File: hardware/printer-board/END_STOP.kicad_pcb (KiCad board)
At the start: 2 copper layers, 18 parts, among them J26 X_MIN, J27 X_MAX, J28 Y_MIN, J29 Y_MAX, J30 Z_MIN, J31 Z_MAX

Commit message: update,
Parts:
- J26, J27, J28, J29, J30, J31: footprint footprint-lib:s3b-ph-kl,end_stop -> footprint-lib:b3b-ph-kl,end_stop
- moved J29 22.7 mm to (27.8, 50.2), turned to 180 degrees
- moved J31 22.1 mm to (38.0, 50.2), turned to 180 degrees
- moved D20 17.5 mm to (43.0, 49.7)
- moved R64 17.5 mm to (43.0, 49.7)
- moved D18 14.0 mm to (33.0, 49.6)
- moved R62 14.0 mm to (33.0, 49.6)
- moved J30 12.7 mm to (38.1, 43.6), turned to 180 degrees
- moved J28 12.3 mm to (27.9, 43.8), turned to 180 degrees
- moved J27 11.7 mm to (27.9, 37.0), turned to 180 degrees
- moved D17 11.5 mm to (33.0, 43.4)
- moved R61 11.5 mm to (33.0, 43.4)
- moved J26 11.0 mm to (28.1, 31.5), turned to 180 degrees
- moved R59 9.83 mm to (33.2, 31.2)
- moved D16 9.66 mm to (33.2, 36.9)
- moved R60 9.66 mm to (33.2, 36.9)
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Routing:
- net +5V: track 51.7 -> 0.00 mm
- net GND: track 51.0 -> 0.00 mm
- net /Y_MIN: track 4.47 -> 0.00 mm
- net /Z_MAX: track 4.26 -> 0.00 mm
- net /Y_MAX: track 4.17 -> 0.00 mm
- net /X_MIN: track 4.16 -> 0.00 mm
- net /Z_MIN: track 3.97 -> 0.00 mm
- net /X_MAX: track 3.55 -> 0.00 mm
- net Net-(D15-Pad2): track 2.98 -> 0.00 mm, vias 1 -> 0
- net Net-(D16-Pad2): track 2.90 -> 0.00 mm, vias 1 -> 0
- net Net-(D18-Pad2): track 2.47 -> 0.00 mm, vias 1 -> 0
- net Net-(D20-Pad2): track 2.27 -> 0.00 mm, vias 1 -> 0
- net Net-(D19-Pad2): track 2.24 -> 0.00 mm, vias 1 -> 0
- net Net-(D17-Pad2): track 2.22 -> 0.00 mm, vias 1 -> 0

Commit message: update for stepper Z,
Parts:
- added C1: CP100uf,35V, Capacitor_SMD:C_0603_1608Metric_Pad1.05x0.95mm_HandSolder, F.Cu at (190.6, 45.3)
- added C10: CP100uf,25V, Capacitor_SMD:CP_Elec_6.3x7.7, F.Cu at (297.3, 53.2)
- added C11: C104,0603, Capacitor_SMD:C_0603_1608Metric_Pad1.05x0.95mm_HandSolder, F.Cu at (297.6, 59.1)
- added C12: CP100uf,25V, Capacitor_SMD:CP_Elec_6.3x7.7, F.Cu at (240.3, 109.1)
- added C13: C104,0603, Capacitor_SMD:C_0603_1608Metric_Pad1.05x0.95mm_HandSolder, F.Cu at (237.3, 115.0)
- added C14: C106,0603, Capacitor_SMD:C_0603_1608Metric_Pad1.05x0.95mm_HandSolder, F.Cu at (295.6, 127.7)
- added C15: C106,0603, Capacitor_SMD:C_0603_1608Metric_Pad1.05x0.95mm_HandSolder, F.Cu at (292.3, 136.8)
- added C16: C106,0603, Capacitor_SMD:C_0603_1608Metric_Pad1.05x0.95mm_HandSolder, F.Cu at (292.3, 127.7)
- added C17: C106,0603, Capacitor_SMD:C_0603_1608Metric_Pad1.05x0.95mm_HandSolder, F.Cu at (295.6, 129.2)
- added C18: C106,0603, Capacitor_SMD:C_0603_1608Metric_Pad1.05x0.95mm_HandSolder, F.Cu at (292.3, 132.3)
- added C19: C104,0603, Capacitor_SMD:C_0603_1608Metric_Pad1.05x0.95mm_HandSolder, F.Cu at (221.4, 140.3)
- added C2: CP100uf,25V, Capacitor_SMD:CP_Elec_6.3x7.7, F.Cu at (160.0, 109.1)
- added C20: CP100uf,35V, Capacitor_SMD:CP_Elec_6.3x7.7, F.Cu at (235.1, 137.6)
- added C21: C104,0603, Capacitor_SMD:C_0603_1608Metric_Pad1.05x0.95mm_HandSolder, F.Cu at (295.3, 86.0)
- added C22: C10pf,0603, Capacitor_SMD:C_0603_1608Metric_Pad1.05x0.95mm_HandSolder, F.Cu at (281.9, 85.8)
- added C23: C104,0603, Capacitor_SMD:C_0603_1608Metric_Pad1.05x0.95mm_HandSolder, F.Cu at (308.3, 76.8)
- added C24: C10pf,0603, Capacitor_SMD:C_0603_1608Metric_Pad1.05x0.95mm_HandSolder, F.Cu at (285.2, 85.8)
- added C25: C104,0603, Capacitor_SMD:C_0603_1608Metric_Pad1.05x0.95mm_HandSolder, F.Cu at (295.1, 82.0)
- added C26: C104,0603, Capacitor_SMD:C_0603_1608Metric_Pad1.05x0.95mm_HandSolder, F.Cu at (295.1, 80.4)
- added C27: C104,0603, Capacitor_SMD:C_0603_1608Metric_Pad1.05x0.95mm_HandSolder, F.Cu at (298.5, 80.4)
- added C28: C104,0603, Capacitor_SMD:C_0603_1608Metric_Pad1.05x0.95mm_HandSolder, F.Cu at (295.1, 83.5)
- added C29: C105,0603, Capacitor_SMD:C_0603_1608Metric_Pad1.05x0.95mm_HandSolder, F.Cu at (305.0, 75.3)
- added C3: C104,0603, Capacitor_SMD:C_0603_1608Metric_Pad1.05x0.95mm_HandSolder, F.Cu at (166.4, 109.9)
- added C30: C104,0603, Capacitor_SMD:C_0603_1608Metric_Pad1.05x0.95mm_HandSolder, F.Cu at (298.5, 78.9)
- added C31: C104,0603, Capacitor_SMD:C_0603_1608Metric_Pad1.05x0.95mm_HandSolder, F.Cu at (291.9, 85.8)
- added C32: C104,0603, Capacitor_SMD:C_0603_1608Metric_Pad1.05x0.95mm_HandSolder, F.Cu at (288.6, 85.8)
- added C33: CP220uf,16V, Capacitor_SMD:C_0603_1608Metric_Pad1.05x0.95mm_HandSolder, F.Cu at (147.7, 149.0)
- added C34: CP220uf,16V, Capacitor_SMD:C_0603_1608Metric_Pad1.05x0.95mm_HandSolder, F.Cu at (144.3, 149.0)
- added C35: CP220uf,25V, Capacitor_SMD:C_0603_1608Metric_Pad1.05x0.95mm_HandSolder, F.Cu at (144.3, 150.5)
- added C36: CP100uf,16V, Capacitor_SMD:CP_Elec_6.3x5.3, F.Cu at (259.2, 130.5)
- added C37: CP100uf,16V, Capacitor_SMD:CP_Elec_6.3x5.3, F.Cu at (321.8, 48.1)
- added C38: CP100uf,16V, Capacitor_SMD:CP_Elec_6.3x5.3, F.Cu at (259.2, 145.1)
- added C39: CP100uf,25V, Capacitor_SMD:CP_Elec_6.3x7.7, F.Cu at (257.2, 77.0)
- added C4: CP100uf,25V, Capacitor_SMD:CP_Elec_6.3x7.7, F.Cu at (200.2, 109.1)
- added C40: C104,0603, Capacitor_SMD:C_0603_1608Metric_Pad1.05x0.95mm_HandSolder, F.Cu at (254.2, 84.5)
- added C41: CP100uf,25V, Capacitor_SMD:CP_Elec_6.3x7.7, F.Cu at (257.2, 53.2)
- added C42: C104,0603, Capacitor_SMD:C_0603_1608Metric_Pad1.05x0.95mm_HandSolder, F.Cu at (263.6, 54.0)
- added C43: C104,0603, Capacitor_SMD:C_0603_1608Metric_Pad1.05x0.95mm_HandSolder, F.Cu at (274.0, 103.0)
- added C44: CP100uf,16V, Capacitor_SMD:CP_Elec_6.3x5.3, F.Cu at (280.3, 95.8)
- added C45: C106,0603, Capacitor_SMD:C_0603_1608Metric_Pad1.05x0.95mm_HandSolder, F.Cu at (318.6, 92.3)
- added C46: C104,0603, Capacitor_SMD:C_0603_1608Metric_Pad1.05x0.95mm_HandSolder, F.Cu at (325.3, 92.3)
- added C47: C332,0603, Capacitor_SMD:C_0603_1608Metric_Pad1.05x0.95mm_HandSolder, F.Cu at (322.0, 92.3)
- added C48: C103,0603, Capacitor_SMD:C_0603_1608Metric_Pad1.05x0.95mm_HandSolder, F.Cu at (318.6, 93.8)
- added C49: C226,6.3v,0603, Capacitor_SMD:C_0603_1608Metric_Pad1.05x0.95mm_HandSolder, F.Cu at (328.7, 93.8)
- added C5: C104,0603, Capacitor_SMD:C_0603_1608Metric_Pad1.05x0.95mm_HandSolder, F.Cu at (197.2, 116.6)
- added C50: C106,0603, Capacitor_SMD:C_0603_1608Metric_Pad1.05x0.95mm_HandSolder, F.Cu at (224.8, 152.9)
- added C51: C104,0603, Capacitor_SMD:C_0603_1608Metric_Pad1.05x0.95mm_HandSolder, F.Cu at (228.1, 151.4)
- added C52: C332,0603, Capacitor_SMD:C_0603_1608Metric_Pad1.05x0.95mm_HandSolder, F.Cu at (221.4, 152.9)
- added C53: C103,0603, Capacitor_SMD:C_0603_1608Metric_Pad1.05x0.95mm_HandSolder, F.Cu at (224.8, 151.4)
- added C54: C226,6.3v,0603, Capacitor_SMD:C_0603_1608Metric_Pad1.05x0.95mm_HandSolder, F.Cu at (221.4, 151.4)
- added C6: CP100uf,25V, Capacitor_SMD:CP_Elec_6.3x7.7, F.Cu at (160.0, 133.1)
- added C7: C104,0603, Capacitor_SMD:C_0603_1608Metric_Pad1.05x0.95mm_HandSolder, F.Cu at (160.3, 139.0)
- added C8: CP100uf,25V, Capacitor_SMD:CP_Elec_6.3x7.7, F.Cu at (200.1, 133.1)
- added C9: C104,0603, Capacitor_SMD:C_0603_1608Metric_Pad1.05x0.95mm_HandSolder, F.Cu at (197.1, 140.5)
- added D1: 5V HEALTHY, LED_SMD:LED_0603_1608Metric_Pad1.05x0.95mm_HandSolder, F.Cu at (141.2, 93.6)
- added D10: LED_BLUE,0603, LED_SMD:LED_0603_1608Metric_Pad1.05x0.95mm_HandSolder, F.Cu at (315.2, 79.3)
- added D11: LED_BLUE,0603, LED_SMD:LED_0603_1608Metric_Pad1.05x0.95mm_HandSolder, F.Cu at (318.6, 79.3)
- added D12: LED_BLUE,0603, LED_SMD:LED_0603_1608Metric_Pad1.05x0.95mm_HandSolder, F.Cu at (318.6, 80.9)
- added D13: LED_BLUE,0603, LED_SMD:LED_0603_1608Metric_Pad1.05x0.95mm_HandSolder, F.Cu at (325.4, 79.3)
- added D14: LED_BLUE,0603, LED_SMD:LED_0603_1608Metric_Pad1.05x0.95mm_HandSolder, F.Cu at (322.0, 79.3)
- added D2: LED_BLUE,0603, LED_SMD:LED_0603_1608Metric_Pad1.05x0.95mm_HandSolder, F.Cu at (157.0, 115.4)
- added D21: LED_BLUE,0603, LED_SMD:LED_0603_1608Metric_Pad1.05x0.95mm_HandSolder, F.Cu at (322.4, 52.4)
- added D22: LED_BLUE,0603, LED_SMD:LED_0603_1608Metric_Pad1.05x0.95mm_HandSolder, F.Cu at (272.1, 142.3)
- added D23: LED_BLUE,0603, LED_SMD:LED_0603_1608Metric_Pad1.05x0.95mm_HandSolder, F.Cu at (254.2, 81.4)
- added D24: LED_BLUE,0603, LED_SMD:LED_0603_1608Metric_Pad1.05x0.95mm_HandSolder, F.Cu at (254.2, 57.5)
- added D3: LED_BLUE,0603, LED_SMD:LED_0603_1608Metric_Pad1.05x0.95mm_HandSolder, F.Cu at (197.2, 113.5)
- added D4: LED_BLUE,0603, LED_SMD:LED_0603_1608Metric_Pad1.05x0.95mm_HandSolder, F.Cu at (157.0, 137.4)
- added D5: LED_BLUE,0603, LED_SMD:LED_0603_1608Metric_Pad1.05x0.95mm_HandSolder, F.Cu at (197.1, 137.4)
- added D6: LED_BLUE,0603, LED_SMD:LED_0603_1608Metric_Pad1.05x0.95mm_HandSolder, F.Cu at (294.3, 57.5)
- added D7: LED_BLUE,0603, LED_SMD:LED_0603_1608Metric_Pad1.05x0.95mm_HandSolder, F.Cu at (237.3, 113.5)
- added D8: LED_RED,0603, LED_SMD:LED_0603_1608Metric_Pad1.05x0.95mm_HandSolder, F.Cu at (295.3, 119.1)
- added D9: LED_BLUE,0603, LED_SMD:LED_0603_1608Metric_Pad1.05x0.95mm_HandSolder, F.Cu at (315.2, 80.9)
- added F1: 16V/30A, w_misc_comp:fuse_smf, F.Cu at (225.0, 127.0)
- added F2: 30V/5A, w_misc_comp:fuse_smf, F.Cu at (225.0, 132.4)
- added H1: MOUNT_M3, MountingHole:MountingHole_2.7mm_M2.5, F.Cu at (3.00, 3.00)
- added H2: MOUNT_M3, MountingHole:MountingHole_2.7mm_M2.5, F.Cu at (97.0, 3.00)
- added H3: MOUNT_M3, MountingHole:MountingHole_2.7mm_M2.5, F.Cu at (3.00, 97.0)
- added H4: MOUNT_M3, MountingHole:MountingHole_2.7mm_M2.5, F.Cu at (97.0, 97.0)
- added J1: USB_DEBUG, Connector_PinHeader_1.27mm:PinHeader_1x05_P1.27mm_Vertical, F.Cu at (187.4, 45.7)
- added J10: MS_SELECT, Connector_PinHeader_2.54mm:PinHeader_2x03_P2.54mm_Vertical, F.Cu at (304.8, 46.3)
- added J11: E0, footprint-lib:b4b-ph-kl,stepper_terminal, F.Cu at (297.8, 46.6)
- added J12: MS_SELECT, Connector_PinHeader_2.54mm:PinHeader_2x03_P2.54mm_Vertical, F.Cu at (247.8, 102.3)
- added J13: E1, footprint-lib:b4b-ph-kl,stepper_terminal, F.Cu at (240.8, 102.6)
- added J14: HEATBED, footprint-lib:mpt_0,5%2f2-2,54,heatbed, F.Cu at (309.5, 113.4)
- added J15: X_MIN, footprint-lib:b3b-ph-kl,end_stop, F.Cu at (317.7, 70.5)
- added J16: X_MAX, footprint-lib:b3b-ph-kl,end_stop, F.Cu at (317.7, 75.6)
- added J17: Y_MIN, footprint-lib:b3b-ph-kl,end_stop, F.Cu at (326.1, 70.5)
- added J18: Y_MAX, footprint-lib:b3b-ph-kl,end_stop, F.Cu at (326.1, 75.6)
- added J19: Z_MIN, footprint-lib:b3b-ph-kl,end_stop, F.Cu at (334.5, 70.5)
- added J2: MS_SELECT, Connector_PinHeader_2.54mm:PinHeader_2x03_P2.54mm_Vertical, F.Cu at (167.5, 102.3)
- added J20: Z_MAX, footprint-lib:b3b-ph-kl,end_stop, F.Cu at (334.5, 75.6)
- added J21: HEATBED_TEMP, w_conn_jst-ph:b2b-ph-kl, F.Cu at (281.1, 134.1)
- added J22: HOTEND_TEMP0, w_conn_jst-ph:b2b-ph-kl, F.Cu at (281.1, 129.1)
- added J23: HOTEND_TEMP1, w_conn_jst-ph:b2b-ph-kl, F.Cu at (287.4, 129.1)
- added J24: AUX_TEMP, w_conn_jst-ph:b2b-ph-kl, F.Cu at (287.4, 134.1)
- added J25: 12V_INPUT_2, footprint-lib:mpt_0,5%2f2-2,54,12V_SRC, F.Cu at (245.3, 130.8)
- added J3: X, footprint-lib:b4b-ph-kl,stepper_terminal, F.Cu at (160.5, 102.6)
- added J32: HOT_END, footprint-lib:mpt_0,5%2f2-2,54,heatbed, F.Cu at (279.6, 116.8)
- added J33: TO FAN0, footprint-lib:b2b-ph-kl,fan_pwm_out, F.Cu at (267.2, 129.1)
- added J34: TO FAN1, footprint-lib:b2b-ph-kl,fan_pwm_out, F.Cu at (329.8, 46.6)
- added J35: TO FAN2, footprint-lib:b2b-ph-kl,fan_pwm_out, F.Cu at (267.2, 143.6)
- added J36: MS_SELECT, Connector_PinHeader_2.54mm:PinHeader_2x03_P2.54mm_Vertical, F.Cu at (264.7, 70.2)
- added J37: Z2, footprint-lib:b4b-ph-kl,stepper_terminal, F.Cu at (257.7, 70.5)
- added J38: MS_SELECT, Connector_PinHeader_2.54mm:PinHeader_2x03_P2.54mm_Vertical, F.Cu at (264.7, 46.3)
- added J39: Y, footprint-lib:b4b-ph-kl,stepper_terminal, F.Cu at (257.7, 46.6)
- added J4: MS_SELECT, Connector_PinHeader_2.54mm:PinHeader_2x03_P2.54mm_Vertical, F.Cu at (207.7, 102.3)
- added J40: Conn_01x07, Connector_PinHeader_1.27mm:PinHeader_1x07_P1.27mm_Vertical, F.Cu at (273.9, 93.4)
- added J41: EXP1, Connector_PinHeader_2.54mm:PinHeader_2x05_P2.54mm_Vertical, F.Cu at (261.8, 94.1)
- added J42: EXP2, Connector_PinHeader_2.54mm:PinHeader_2x05_P2.54mm_Vertical, F.Cu at (268.0, 94.1)
- added J5: Z, footprint-lib:b4b-ph-kl,stepper_terminal, F.Cu at (200.7, 102.6)
- added J6: MS_SELECT, Connector_PinHeader_2.54mm:PinHeader_2x03_P2.54mm_Vertical, F.Cu at (167.5, 126.2)
- added J7: Z1, footprint-lib:b4b-ph-kl,stepper_terminal, F.Cu at (160.5, 126.5)
- added J8: MS_SELECT, Connector_PinHeader_2.54mm:PinHeader_2x03_P2.54mm_Vertical, F.Cu at (207.6, 126.2)
- added J9: Z3, footprint-lib:b4b-ph-kl,stepper_terminal, F.Cu at (200.6, 126.5)
- added JP1: Jumper_NO_Small, Jumper:SolderJumper-2_P1.3mm_Open_TrianglePad1.0x1.5mm, F.Cu at (141.2, 95.7)
- added JP2: Jumper_NO_Small, Jumper:SolderJumper-2_P1.3mm_Open_TrianglePad1.0x1.5mm, F.Cu at (187.5, 54.7)
- added JP3: Jumper_NO_Small, Jumper:SolderJumper-2_P1.3mm_Open_TrianglePad1.0x1.5mm, F.Cu at (194.0, 45.8)
- added JP4: Jumper_NO_Small, Jumper:SolderJumper-2_P1.3mm_Open_TrianglePad1.0x1.5mm, F.Cu at (144.6, 94.1)
- added JP5: Jumper_NO_Small, SolderJumper-2_P1.3mm_Open_TrianglePad1.0x1.5mm, F.Cu at (221.4, 138.3)
- added JP6: Jumper_NO_Small, SolderJumper-2_P1.3mm_Open_TrianglePad1.0x1.5mm, F.Cu at (298.5, 84.0)
- added JP7: Jumper_NO_Small, SolderJumper-2_P1.3mm_Open_TrianglePad1.0x1.5mm, F.Cu at (305.2, 78.8)
- added L1: L_Small, w_smd_inductors:inductor_smd_0603, F.Cu at (301.3, 83.4)
- added L2: L_15uH, w_smd_inductors:inductor_smd_4.8x2.8mm, F.Cu at (327.2, 88.8)
- added L3: L_15uH, w_smd_inductors:inductor_smd_4.8x2.8mm, F.Cu at (229.9, 147.9)
- added Q1: WSK220N04, footprint-lib:TO-263-2,drill_array, F.Cu at (298.1, 112.6)
- added Q2: STP55NF06, footprint-lib:TO-263-2,drill_array, F.Cu at (298.1, 96.0)
- added Q3: STP55NF06, footprint-lib:TO-263-2,drill_array, F.Cu at (268.3, 116.0)
- added Q4: D882, footprint-lib:SOT-89-3,thermal_vias, F.Cu at (266.5, 134.6)
- added Q5: D882, footprint-lib:SOT-89-3,thermal_vias, F.Cu at (329.1, 52.2)
- added Q6: D882, footprint-lib:SOT-89-3,thermal_vias, F.Cu at (266.5, 149.2)
- added R1: R153,0603, Resistor_SMD:R_0603_1608Metric_Pad1.05x0.95mm_HandSolder, F.Cu at (238.4, 94.5)
- added R10: R103,0603, Resistor_SMD:R_0603_1608Metric_Pad1.05x0.95mm_HandSolder, F.Cu at (160.4, 115.4)
- added R11: R104,0603, Resistor_SMD:R_0603_1608Metric_Pad1.05x0.95mm_HandSolder, F.Cu at (197.2, 115.0)
- added R12: R102,0603, Resistor_SMD:R_0603_1608Metric_Pad1.05x0.95mm_HandSolder, F.Cu at (206.6, 109.9)
- added R13: R103,0603, Resistor_SMD:R_0603_1608Metric_Pad1.05x0.95mm_HandSolder, F.Cu at (200.5, 115.0)
- added R14: R104,0603, Resistor_SMD:R_0603_1608Metric_Pad1.05x0.95mm_HandSolder, F.Cu at (166.4, 133.9)
- added R15: R102,0603, Resistor_SMD:R_0603_1608Metric_Pad1.05x0.95mm_HandSolder, F.Cu at (157.0, 139.0)
- added R16: R103,0603, Resistor_SMD:R_0603_1608Metric_Pad1.05x0.95mm_HandSolder, F.Cu at (157.0, 140.5)
- added R17: R104,0603, Resistor_SMD:R_0603_1608Metric_Pad1.05x0.95mm_HandSolder, F.Cu at (197.1, 139.0)
- added R18: R102,0603, Resistor_SMD:R_0603_1608Metric_Pad1.05x0.95mm_HandSolder, F.Cu at (206.5, 133.9)
- added R19: R103,0603, Resistor_SMD:R_0603_1608Metric_Pad1.05x0.95mm_HandSolder, F.Cu at (200.4, 139.0)
- added R2: R153,0603, Resistor_SMD:R_0603_1608Metric_Pad1.05x0.95mm_HandSolder, F.Cu at (238.4, 93.0)
- added R20: R104,0603, Resistor_SMD:R_0603_1608Metric_Pad1.05x0.95mm_HandSolder, F.Cu at (303.7, 54.0)
- added R21: R102,0603, Resistor_SMD:R_0603_1608Metric_Pad1.05x0.95mm_HandSolder, F.Cu at (294.3, 60.6)
- added R22: R103,0603, Resistor_SMD:R_0603_1608Metric_Pad1.05x0.95mm_HandSolder, F.Cu at (294.3, 59.1)
- added R23: R104,0603, Resistor_SMD:R_0603_1608Metric_Pad1.05x0.95mm_HandSolder, F.Cu at (240.6, 115.0)
- added R24: R102,0603, Resistor_SMD:R_0603_1608Metric_Pad1.05x0.95mm_HandSolder, F.Cu at (246.7, 109.9)
- added R25: R103,0603, Resistor_SMD:R_0603_1608Metric_Pad1.05x0.95mm_HandSolder, F.Cu at (237.3, 116.6)
- added R26: R100,0805, Resistor_SMD:R_0805_2012Metric_Pad1.15x1.40mm_HandSolder, F.Cu at (308.3, 117.6)
- added R27: R104,0805, Resistor_SMD:R_0805_2012Metric_Pad1.15x1.40mm_HandSolder, F.Cu at (291.7, 119.3)
- added R28: R182,0603, Resistor_SMD:R_0603_1608Metric_Pad1.05x0.95mm_HandSolder, F.Cu at (298.6, 119.0)
- added R29: R102,0603, Resistor_SMD:R_0603_1608Metric_Pad1.05x0.95mm_HandSolder, F.Cu at (332.0, 82.3)
- added R3: R152,0603, Resistor_SMD:R_0603_1608Metric_Pad1.05x0.95mm_HandSolder, F.Cu at (241.7, 93.0)
- added R30: R102,0603, Resistor_SMD:R_0603_1608Metric_Pad1.05x0.95mm_HandSolder, F.Cu at (328.7, 79.3)
- added R31: R102,0603, Resistor_SMD:R_0603_1608Metric_Pad1.05x0.95mm_HandSolder, F.Cu at (325.3, 80.9)
- added R32: R102,0603, Resistor_SMD:R_0603_1608Metric_Pad1.05x0.95mm_HandSolder, F.Cu at (328.7, 80.8)
- added R33: R102,0603, Resistor_SMD:R_0603_1608Metric_Pad1.05x0.95mm_HandSolder, F.Cu at (328.7, 82.3)
- added R34: R102,0603, Resistor_SMD:R_0603_1608Metric_Pad1.05x0.95mm_HandSolder, F.Cu at (322.0, 80.9)
- added R35: R472,0603, Resistor_SMD:R_0603_1608Metric_Pad1.05x0.95mm_HandSolder, F.Cu at (292.3, 129.2)
- added R36: R472,0603, Resistor_SMD:R_0603_1608Metric_Pad1.05x0.95mm_HandSolder, F.Cu at (292.3, 130.7)
- added R37: R472,0603, Resistor_SMD:R_0603_1608Metric_Pad1.05x0.95mm_HandSolder, F.Cu at (292.3, 135.3)
- added R38: R472,0603, Resistor_SMD:R_0603_1608Metric_Pad1.05x0.95mm_HandSolder, F.Cu at (295.6, 132.3)
- added R39: R472,0603, Resistor_SMD:R_0603_1608Metric_Pad1.05x0.95mm_HandSolder, F.Cu at (292.3, 133.8)
- added R4: R220,0603, Resistor_SMD:R_0603_1608Metric_Pad1.05x0.95mm_HandSolder, F.Cu at (187.5, 52.7)
- added R40: R472,0603, Resistor_SMD:R_0603_1608Metric_Pad1.05x0.95mm_HandSolder, F.Cu at (301.8, 82.0)
- added R41: R472,0603, Resistor_SMD:R_0603_1608Metric_Pad1.05x0.95mm_HandSolder, F.Cu at (301.8, 80.4)
- added R42: R0,0603, Resistor_SMD:R_0603_1608Metric_Pad1.05x0.95mm_HandSolder, F.Cu at (308.3, 75.3)
- added R43: R0,0603, Resistor_SMD:R_0603_1608Metric_Pad1.05x0.95mm_HandSolder, F.Cu at (295.1, 78.9)
- added R44: R102,0603, Resistor_SMD:R_0603_1608Metric_Pad1.05x0.95mm_HandSolder, F.Cu at (301.8, 78.9)
- added R45: R103,0603, Resistor_SMD:R_0603_1608Metric_Pad1.05x0.95mm_HandSolder, F.Cu at (305.0, 76.8)
- added R46: R103,0603, Resistor_SMD:R_0603_1608Metric_Pad1.05x0.95mm_HandSolder, F.Cu at (298.5, 82.0)
- added R47: R220,0603, Resistor_SMD:R_0603_1608Metric_Pad1.05x0.95mm_HandSolder, F.Cu at (160.7, 150.5)
- added R48: R220,0603, Resistor_SMD:R_0603_1608Metric_Pad1.05x0.95mm_HandSolder, F.Cu at (164.0, 149.0)
- added R49: R152,0603, Resistor_SMD:R_0603_1608Metric_Pad1.05x0.95mm_HandSolder, F.Cu at (160.7, 149.0)
- added R5: R220,0603, Resistor_SMD:R_0603_1608Metric_Pad1.05x0.95mm_HandSolder, F.Cu at (147.9, 93.6)
- added R50: R100,0805, Resistor_SMD:R_0805_2012Metric_Pad1.15x1.40mm_HandSolder, F.Cu at (308.3, 101.0)
- added R51: R104,0805, Resistor_SMD:R_0805_2012Metric_Pad1.15x1.40mm_HandSolder, F.Cu at (291.7, 102.7)
- added R52: R182,0603, Resistor_SMD:R_0603_1608Metric_Pad1.05x0.95mm_HandSolder, F.Cu at (298.6, 102.4)
- added R53: R100,0805, Resistor_SMD:R_0805_2012Metric_Pad1.15x1.40mm_HandSolder, F.Cu at (261.8, 122.7)
- added R54: R104,0805, Resistor_SMD:R_0805_2012Metric_Pad1.15x1.40mm_HandSolder, F.Cu at (278.5, 121.0)
- added R55: R182,0603, Resistor_SMD:R_0603_1608Metric_Pad1.05x0.95mm_HandSolder, F.Cu at (268.8, 122.5)
- added R56: R100,0805, Resistor_SMD:R_0805_2012Metric_Pad1.15x1.40mm_HandSolder, F.Cu at (272.3, 127.9)
- added R57: R104,0805, Resistor_SMD:R_0805_2012Metric_Pad1.15x1.40mm_HandSolder, F.Cu at (256.2, 135.1)
- added R58: R100,0603, Resistor_SMD:R_0603_1608Metric_Pad1.05x0.95mm_HandSolder, F.Cu at (259.4, 136.8)
- added R6: R152,0603, Resistor_SMD:R_0603_1608Metric_Pad1.05x0.95mm_HandSolder, F.Cu at (190.6, 48.3)
- added R65: R104,0805, Resistor_SMD:R_0805_2012Metric_Pad1.15x1.40mm_HandSolder, F.Cu at (256.2, 149.6)
- added R66: R100,0603, Resistor_SMD:R_0603_1608Metric_Pad1.05x0.95mm_HandSolder, F.Cu at (256.0, 151.4)
- added R67: R182,0603, Resistor_SMD:R_0603_1608Metric_Pad1.05x0.95mm_HandSolder, F.Cu at (259.4, 151.4)
- added R68: R104,0603, Resistor_SMD:R_0603_1608Metric_Pad1.05x0.95mm_HandSolder, F.Cu at (257.5, 83.0)
- added R69: R102,0603, Resistor_SMD:R_0603_1608Metric_Pad1.05x0.95mm_HandSolder, F.Cu at (254.2, 83.0)
- added R7: R102,0603, Resistor_SMD:R_0603_1608Metric_Pad1.05x0.95mm_HandSolder, F.Cu at (190.6, 46.8)
- added R70: R103,0603, Resistor_SMD:R_0603_1608Metric_Pad1.05x0.95mm_HandSolder, F.Cu at (263.6, 77.8)
- added R71: R104,0603, Resistor_SMD:R_0603_1608Metric_Pad1.05x0.95mm_HandSolder, F.Cu at (257.5, 59.1)
- added R72: R102,0603, Resistor_SMD:R_0603_1608Metric_Pad1.05x0.95mm_HandSolder, F.Cu at (254.2, 60.6)
- added R73: R103,0603, Resistor_SMD:R_0603_1608Metric_Pad1.05x0.95mm_HandSolder, F.Cu at (254.2, 59.1)
- added R74: R562,0603, Resistor_SMD:R_0603_1608Metric_Pad1.05x0.95mm_HandSolder, F.Cu at (328.7, 92.3)
- added R75: R103,0603, Resistor_SMD:R_0603_1608Metric_Pad1.05x0.95mm_HandSolder, F.Cu at (325.3, 93.8)
- added R76: R333,0603, Resistor_SMD:R_0603_1608Metric_Pad1.05x0.95mm_HandSolder, F.Cu at (322.0, 93.8)
- added R77: R562,0603, Resistor_SMD:R_0603_1608Metric_Pad1.05x0.95mm_HandSolder, F.Cu at (228.1, 152.9)
- added R78: R103,0603, Resistor_SMD:R_0603_1608Metric_Pad1.05x0.95mm_HandSolder, F.Cu at (231.5, 151.4)
- added R79: R333,0603, Resistor_SMD:R_0603_1608Metric_Pad1.05x0.95mm_HandSolder, F.Cu at (231.5, 152.9)
- added R8: R104,0603, Resistor_SMD:R_0805_2012Metric_Pad1.15x1.40mm_HandSolder, F.Cu at (157.2, 113.7)
- added R9: R102,0603, Resistor_SMD:R_0603_1608Metric_Pad1.05x0.95mm_HandSolder, F.Cu at (157.0, 117.0)
- added SW1: SW_Push, Button_Switch_SMD:SW_SPST_CK_RS282G05A3, F.Cu at (298.4, 76.1)
- added TH1: Thermistor_NTC, Resistor_SMD:R_0603_1608Metric_Pad1.05x0.95mm_HandSolder, F.Cu at (295.6, 130.7)
- added U1: orange_pi_zero, footprint-lib:orangepi-zero, F.Cu at (139.8, 92.6)
- added U10: A4988_MODULE, footprint-lib:Pololu_Breakout-16_15.2x20.3mm, F.Cu at (238.2, 46.0)
- added U11: MP2303A_ALT, footprint-lib:SOIC-8_3.9x4.9mm_P1.27mm,thermal_via, F.Cu at (320.7, 88.8)
- added U12: MP2303A_ALT, footprint-lib:SOIC-8_3.9x4.9mm_P1.27mm,thermal_via, F.Cu at (223.5, 147.9)
- added U2: A4988_MODULE, footprint-lib:Pololu_Breakout-16_15.2x20.3mm, F.Cu at (141.1, 102.0)
- added U3: A4988_MODULE, footprint-lib:Pololu_Breakout-16_15.2x20.3mm, F.Cu at (181.3, 102.0)
- added U4: A4988_MODULE, footprint-lib:Pololu_Breakout-16_15.2x20.3mm, F.Cu at (141.1, 125.9)
- added U5: A4988_MODULE, footprint-lib:Pololu_Breakout-16_15.2x20.3mm, F.Cu at (181.2, 125.9)
- added U6: A4988_MODULE, footprint-lib:Pololu_Breakout-16_15.2x20.3mm, F.Cu at (278.4, 46.0)
- added U7: A4988_MODULE, footprint-lib:Pololu_Breakout-16_15.2x20.3mm, F.Cu at (221.4, 102.0)
- added U8: STM32F407VET6, w_smd_lqfp:TQFP-100, F.Cu at (285.1, 76.7)
- added U9: A4988_MODULE, footprint-lib:Pololu_Breakout-16_15.2x20.3mm, F.Cu at (238.2, 69.9)
- added Y1: O_8M, Crystal:Crystal_HC49-4H_Vertical, F.Cu at (297.1, 71.2)
- D15, D16: value LED_BLUE,0603 -> SD_M4; footprint LED_SMD:LED_0603_1608Metric_Pad1.05x0.95mm_HandSolder -> Diode_SMD:D_SOD-323_HandSoldering
- D17: value LED_BLUE,0603 -> PB9
- D18, D19: value LED_BLUE,0603 -> LED_RED,0603
- J26: value X_MIN -> 12V_INPUT; footprint footprint-lib:b3b-ph-kl,end_stop -> footprint-lib:mpt_0,5%2f2-2,54,12V_SRC
- J27: value X_MAX -> 12V_OUT; footprint footprint-lib:b3b-ph-kl,end_stop -> footprint-lib:mpt_0,5%2f2-2,54,12V_SRC
- J28: value Y_MIN -> SWD; footprint footprint-lib:b3b-ph-kl,end_stop -> Connector_PinHeader_1.27mm:PinHeader_1x04_P1.27mm_Vertical
- J29: value Y_MAX -> USB_DEBUG; footprint footprint-lib:b3b-ph-kl,end_stop -> Connector_PinHeader_1.27mm:PinHeader_1x05_P1.27mm_Vertical
- J30: value Z_MIN -> PWR_DEBUG; footprint footprint-lib:b3b-ph-kl,end_stop -> Connector_PinHeader_1.27mm:PinHeader_1x05_P1.27mm_Vertical
- J31: value Z_MAX -> HOT_END; footprint footprint-lib:b3b-ph-kl,end_stop -> footprint-lib:mpt_0,5%2f2-2,54,heatbed
- R59, R63: value R102,0603 -> R182,0603; moved to F.Cu
- R60: value R102,0603 -> R100,0805; footprint Resistor_SMD:R_0603_1608Metric_Pad1.05x0.95mm_HandSolder -> Resistor_SMD:R_0805_2012Metric_Pad1.15x1.40mm_HandSolder; moved to F.Cu
- R61: value R102,0603 -> R104,0805; footprint Resistor_SMD:R_0603_1608Metric_Pad1.05x0.95mm_HandSolder -> Resistor_SMD:R_0805_2012Metric_Pad1.15x1.40mm_HandSolder; moved to F.Cu
- R62: value R102,0603 -> R100,0603; moved to F.Cu
- R64: value R102,0603 -> R100,0805; moved to F.Cu
- moved R60 301.8 mm to (334.8, 45.5), turned to 0 degrees
- moved R61 286.0 mm to (318.8, 52.6), turned to 0 degrees
- moved R62 285.6 mm to (318.6, 54.4), turned to 0 degrees
- moved J28 280.5 mm to (307.2, 69.6), turned to 0 degrees
- moved R63 279.0 mm to (322.0, 54.4), turned to 0 degrees
- moved J31 275.4 mm to (309.5, 96.8), turned to 0 degrees
- moved D18 267.5 mm to (295.3, 102.5), turned to 0 degrees
- moved D17 249.2 mm to (278.5, 85.8), turned to 0 degrees
- moved R59 246.6 mm to (256.0, 136.8), turned to 0 degrees
- moved R64 238.6 mm to (259.8, 149.4), turned to 0 degrees
- moved D19 236.0 mm to (265.4, 122.5), turned to 0 degrees
- moved J26 233.4 mm to (239.3, 130.8), turned to 0 degrees
- moved D20 232.9 mm to (259.8, 134.9), turned to 0 degrees
- moved J27 225.9 mm to (233.3, 130.8), turned to 0 degrees
- moved D16 216.6 mm to (225.8, 136.1), turned to 0 degrees
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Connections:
- D15 pad 1: GND -> +12V
- D15 pad 2: Net-(D15-Pad2) -> GND
- D16 pad 1: GND -> /POWER_SUPPLY/AM-VIN
- D16 pad 2: Net-(D16-Pad2) -> +12V
- D17 pad 1: GND -> Net-(D17-Pad1)
- D17 pad 2: Net-(D17-Pad2) -> +3V3
- D18 pad 1: GND -> /HOTENDS/HOTEND_0/-12V
- D19 pad 1: GND -> /HOTENDS/HOTEND_1/-12V
- D20 pad 1: GND -> Net-(D20-Pad1)
- J26 pad 1: /X_MIN -> Net-(F2-Pad1)
- J27 pad 1: /X_MAX -> +12V
- J28 pad 1: /Y_MIN -> GND
- J28 pad 2: GND -> /STM32_CORE/STM32_CORE_MCU/SWCLK
- J28 pad 3: +5V -> /STM32_CORE/STM32_CORE_MCU/SWDIO
- J29 pad 1: /Y_MAX -> +3V3
- J29 pad 2: GND -> Net-(J29-Pad2)
- J29 pad 3: +5V -> Net-(J29-Pad3)
- J30 pad 1: /Z_MIN -> GND
- J30 pad 2: GND -> +3V3
- J30 pad 3: +5V -> +3V3
- J31 pad 1: /Z_MAX -> +12V
- J31 pad 2: GND -> /HOTENDS/HOTEND_0/-12V
- R59 pad 1: /X_MIN -> Net-(D20-Pad2)
- R59 pad 2: Net-(D15-Pad2) -> +12V
- R60 pad 1: /X_MAX -> Net-(Q5-Pad1)
- R60 pad 2: Net-(D16-Pad2) -> /FANS/FAN1/FAN_EN
- R61 pad 1: /Y_MIN -> GND
- R61 pad 2: Net-(D17-Pad2) -> /FANS/FAN1/FAN_EN
- R62 pad 1: /Y_MAX -> Net-(D21-Pad1)
- R62 pad 2: Net-(D18-Pad2) -> Net-(Q5-Pad2)
- R63 pad 1: /Z_MIN -> Net-(D21-Pad2)
- R63 pad 2: Net-(D19-Pad2) -> +12V
- R64 pad 1: /Z_MAX -> Net-(Q6-Pad1)
- R64 pad 2: Net-(D20-Pad2) -> /FANS/FAN2/FAN_EN
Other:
- board outline added: 100 x 100 mm

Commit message: update,
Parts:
- removed C1: CP100uf,35V, Capacitor_SMD:C_0603_1608Metric_Pad1.05x0.95mm_HandSolder
- removed C10, C12, C2, C39, C4, C41, C6, C8: CP100uf,25V, Capacitor_SMD:CP_Elec_6.3x7.7
- removed C11, C13, C19, C21, C23, C25, C26, C27, C28, C3, C30, C31, C32, C40, C42, C43, C46, C5, C51, C7, C9: C104,0603, Capacitor_SMD:C_0603_1608Metric_Pad1.05x0.95mm_HandSolder
- removed C14, C15, C16, C17, C18, C45, C50: C106,0603, Capacitor_SMD:C_0603_1608Metric_Pad1.05x0.95mm_HandSolder
- removed C20: CP100uf,35V, Capacitor_SMD:CP_Elec_6.3x7.7
- removed C22, C24: C10pf,0603, Capacitor_SMD:C_0603_1608Metric_Pad1.05x0.95mm_HandSolder
- removed C29: C105,0603, Capacitor_SMD:C_0603_1608Metric_Pad1.05x0.95mm_HandSolder
- removed C33, C34: CP220uf,16V, Capacitor_SMD:C_0603_1608Metric_Pad1.05x0.95mm_HandSolder
- removed C35: CP220uf,25V, Capacitor_SMD:C_0603_1608Metric_Pad1.05x0.95mm_HandSolder
- removed C36, C37, C38, C44: CP100uf,16V, Capacitor_SMD:CP_Elec_6.3x5.3
- removed C47, C52: C332,0603, Capacitor_SMD:C_0603_1608Metric_Pad1.05x0.95mm_HandSolder
- removed C48, C53: C103,0603, Capacitor_SMD:C_0603_1608Metric_Pad1.05x0.95mm_HandSolder
- removed C49, C54: C226,6.3v,0603, Capacitor_SMD:C_0603_1608Metric_Pad1.05x0.95mm_HandSolder
- removed D1: 5V HEALTHY, LED_SMD:LED_0603_1608Metric_Pad1.05x0.95mm_HandSolder
- removed D15, D16: SD_M4, Diode_SMD:D_SOD-323_HandSoldering
- removed D17: PB9, LED_SMD:LED_0603_1608Metric_Pad1.05x0.95mm_HandSolder
- removed D18, D19, D8: LED_RED,0603, LED_SMD:LED_0603_1608Metric_Pad1.05x0.95mm_HandSolder
- removed D2, D20, D21, D22, D23, D24, D3, D4, D5, D6, D7: LED_BLUE,0603, LED_SMD:LED_0603_1608Metric_Pad1.05x0.95mm_HandSolder
- removed F1: 16V/30A, w_misc_comp:fuse_smf
- removed F2: 30V/5A, w_misc_comp:fuse_smf
- removed H1, H2, H3, H4: MOUNT_M3, MountingHole:MountingHole_2.7mm_M2.5
- removed J1, J29: USB_DEBUG, Connector_PinHeader_1.27mm:PinHeader_1x05_P1.27mm_Vertical
- removed J10, J12, J2, J36, J38, J4, J6, J8: MS_SELECT, Connector_PinHeader_2.54mm:PinHeader_2x03_P2.54mm_Vertical
- removed J11: E0, footprint-lib:b4b-ph-kl,stepper_terminal
- removed J13: E1, footprint-lib:b4b-ph-kl,stepper_terminal
- removed J14: HEATBED, footprint-lib:mpt_0,5%2f2-2,54,heatbed
- removed J21: HEATBED_TEMP, w_conn_jst-ph:b2b-ph-kl
- removed J22: HOTEND_TEMP0, w_conn_jst-ph:b2b-ph-kl
- removed J23: HOTEND_TEMP1, w_conn_jst-ph:b2b-ph-kl
- removed J24: AUX_TEMP, w_conn_jst-ph:b2b-ph-kl
- removed J25: 12V_INPUT_2, footprint-lib:mpt_0,5%2f2-2,54,12V_SRC
- removed J26: 12V_INPUT, footprint-lib:mpt_0,5%2f2-2,54,12V_SRC
- removed J27: 12V_OUT, footprint-lib:mpt_0,5%2f2-2,54,12V_SRC
- removed J28: SWD, Connector_PinHeader_1.27mm:PinHeader_1x04_P1.27mm_Vertical
- removed J3: X, footprint-lib:b4b-ph-kl,stepper_terminal
- removed J30: PWR_DEBUG, Connector_PinHeader_1.27mm:PinHeader_1x05_P1.27mm_Vertical
- removed J31, J32: HOT_END, footprint-lib:mpt_0,5%2f2-2,54,heatbed
- removed J33: TO FAN0, footprint-lib:b2b-ph-kl,fan_pwm_out
- removed J34: TO FAN1, footprint-lib:b2b-ph-kl,fan_pwm_out
- removed J35: TO FAN2, footprint-lib:b2b-ph-kl,fan_pwm_out
- removed J37: Z2, footprint-lib:b4b-ph-kl,stepper_terminal
- removed J39: Y, footprint-lib:b4b-ph-kl,stepper_terminal
- removed J40: Conn_01x07, Connector_PinHeader_1.27mm:PinHeader_1x07_P1.27mm_Vertical
- removed J41: EXP1, Connector_PinHeader_2.54mm:PinHeader_2x05_P2.54mm_Vertical
- removed J42: EXP2, Connector_PinHeader_2.54mm:PinHeader_2x05_P2.54mm_Vertical
- removed J5: Z, footprint-lib:b4b-ph-kl,stepper_terminal
- removed J7: Z1, footprint-lib:b4b-ph-kl,stepper_terminal
- removed J9: Z3, footprint-lib:b4b-ph-kl,stepper_terminal
- removed JP1, JP2, JP3, JP4: Jumper_NO_Small, Jumper:SolderJumper-2_P1.3mm_Open_TrianglePad1.0x1.5mm
- removed JP5, JP6, JP7: Jumper_NO_Small, SolderJumper-2_P1.3mm_Open_TrianglePad1.0x1.5mm
- removed L1: L_Small, w_smd_inductors:inductor_smd_0603
- removed L2, L3: L_15uH, w_smd_inductors:inductor_smd_4.8x2.8mm
- removed Q1: WSK220N04, footprint-lib:TO-263-2,drill_array
- removed Q2, Q3: STP55NF06, footprint-lib:TO-263-2,drill_array
- removed Q4, Q5, Q6: D882, footprint-lib:SOT-89-3,thermal_vias
- removed R1, R2: R153,0603, Resistor_SMD:R_0603_1608Metric_Pad1.05x0.95mm_HandSolder
- removed R10, R13, R16, R19, R22, R25, R45, R46, R70, R73, R75, R78: R103,0603, Resistor_SMD:R_0603_1608Metric_Pad1.05x0.95mm_HandSolder
- removed R11, R14, R17, R20, R23, R68, R71: R104,0603, Resistor_SMD:R_0603_1608Metric_Pad1.05x0.95mm_HandSolder
- removed R12, R15, R18, R21, R24, R44, R69, R7, R72, R9: R102,0603, Resistor_SMD:R_0603_1608Metric_Pad1.05x0.95mm_HandSolder
- removed R26, R50, R53, R56, R60: R100,0805, Resistor_SMD:R_0805_2012Metric_Pad1.15x1.40mm_HandSolder
- removed R27, R51, R54, R57, R61, R65: R104,0805, Resistor_SMD:R_0805_2012Metric_Pad1.15x1.40mm_HandSolder
- removed R28, R52, R55, R59, R63, R67: R182,0603, Resistor_SMD:R_0603_1608Metric_Pad1.05x0.95mm_HandSolder
- removed R3, R49, R6: R152,0603, Resistor_SMD:R_0603_1608Metric_Pad1.05x0.95mm_HandSolder
- removed R35, R36, R37, R38, R39, R40, R41: R472,0603, Resistor_SMD:R_0603_1608Metric_Pad1.05x0.95mm_HandSolder
- removed R4, R47, R48, R5: R220,0603, Resistor_SMD:R_0603_1608Metric_Pad1.05x0.95mm_HandSolder
- removed R42, R43: R0,0603, Resistor_SMD:R_0603_1608Metric_Pad1.05x0.95mm_HandSolder
- removed R58, R62, R66: R100,0603, Resistor_SMD:R_0603_1608Metric_Pad1.05x0.95mm_HandSolder
- removed R64: R100,0805, Resistor_SMD:R_0603_1608Metric_Pad1.05x0.95mm_HandSolder
- removed R74, R77: R562,0603, Resistor_SMD:R_0603_1608Metric_Pad1.05x0.95mm_HandSolder
- removed R76, R79: R333,0603, Resistor_SMD:R_0603_1608Metric_Pad1.05x0.95mm_HandSolder
- removed R8: R104,0603, Resistor_SMD:R_0805_2012Metric_Pad1.15x1.40mm_HandSolder
- removed SW1: SW_Push, Button_Switch_SMD:SW_SPST_CK_RS282G05A3
- removed TH1: Thermistor_NTC, Resistor_SMD:R_0603_1608Metric_Pad1.05x0.95mm_HandSolder
- removed U1: orange_pi_zero, footprint-lib:orangepi-zero
- removed U10, U2, U3, U4, U5, U6, U7, U9: A4988_MODULE, footprint-lib:Pololu_Breakout-16_15.2x20.3mm
- removed U11, U12: MP2303A_ALT, footprint-lib:SOIC-8_3.9x4.9mm_P1.27mm,thermal_via
- removed U8: STM32F407VET6, w_smd_lqfp:TQFP-100
- removed Y1: O_8M, Crystal:Crystal_HC49-4H_Vertical
- R29, R30, R31, R32, R33, R34: moved to B.Cu
- moved R29 331.0 mm to (10.5, 3.50), turned to 90 degrees
- moved J18 326.2 mm to (5.00, 18.0)
- moved J17 326.2 mm to (5.00, 13.0)
- moved R30 326.0 mm to (10.5, 8.50), turned to 90 degrees
- moved R32 324.3 mm to (10.5, 18.5), turned to 90 degrees
- moved J20 322.6 mm to (17.0, 18.0)
- moved J19 322.6 mm to (17.0, 13.0)
- moved R31 321.9 mm to (10.5, 13.5), turned to 90 degrees
- moved J16 319.9 mm to (5.00, 8.00)
- moved J15 319.9 mm to (5.00, 3.00)
- moved D11 315.1 mm to (10.5, 13.5), turned to 90 degrees
- moved D9 314.4 mm to (10.5, 3.50), turned to 90 degrees
- moved D12 314.4 mm to (10.5, 18.5), turned to 90 degrees
- moved R33 313.8 mm to (22.5, 13.5), turned to 90 degrees
- moved D10 312.8 mm to (10.5, 8.50), turned to 90 degrees
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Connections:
- net +3V3 renamed +3V3_STM32
- net /END_STOP/X_MAX renamed /X_MAX
- net /END_STOP/X_MIN renamed /X_MIN
- net /END_STOP/Y_MAX renamed /Y_MAX
- net /END_STOP/Y_MIN renamed /Y_MIN
- net /END_STOP/Z_MAX renamed /Z_MAX
- net /END_STOP/Z_MIN renamed /Z_MIN
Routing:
- net +3V3_STM32: track 0.00 -> 50.7 mm
- net GND: track 0.00 -> 20.0 mm
- net /Z_MIN: track 0.00 -> 7.88 mm
- net /Z_MAX: track 0.00 -> 7.88 mm
- net /Y_MAX: track 0.00 -> 7.88 mm
- net /Y_MIN: track 0.00 -> 7.88 mm
- net /X_MIN: track 0.00 -> 7.88 mm
- net /X_MAX: track 0.00 -> 7.88 mm
- net Net-(D10-Pad2): track 0.00 -> 3.25 mm, vias 0 -> 1
- net Net-(D14-Pad2): track 0.00 -> 2.96 mm, vias 0 -> 1
- net Net-(D12-Pad2): track 0.00 -> 2.24 mm, vias 0 -> 1
- net Net-(D13-Pad2): track 0.00 -> 2.21 mm, vias 0 -> 1
- net Net-(D9-Pad2): track 0.00 -> 2.21 mm, vias 0 -> 1
- net Net-(D11-Pad2): track 0.00 -> 2.21 mm, vias 0 -> 1
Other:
- board outline removed

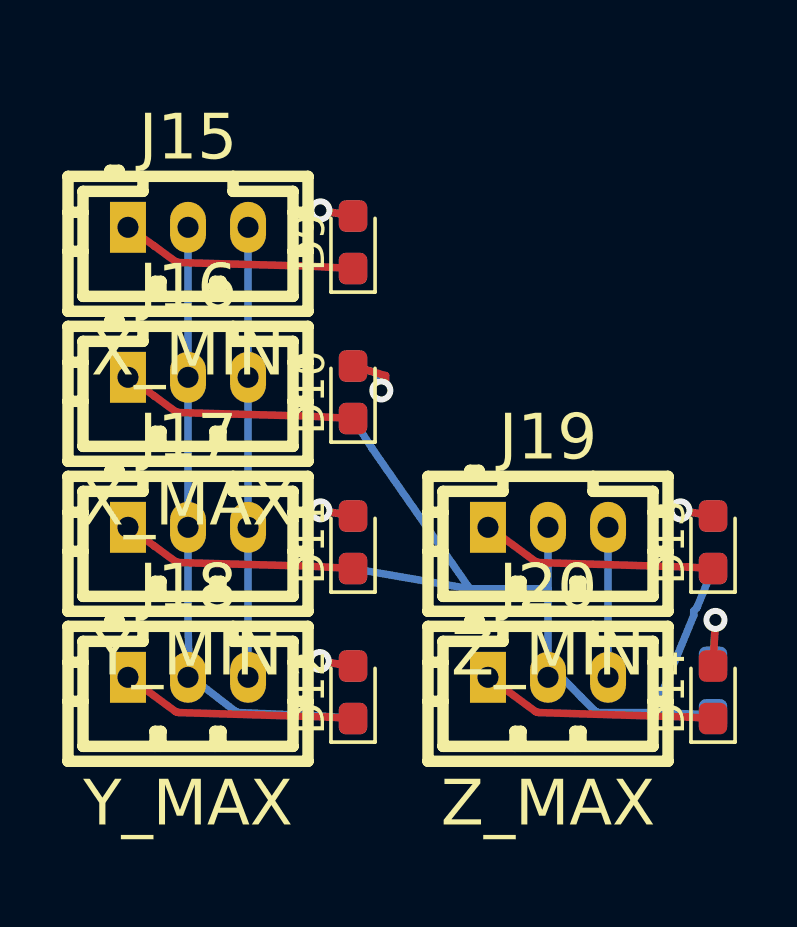
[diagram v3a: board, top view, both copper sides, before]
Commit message: update step motor terminal orientation,
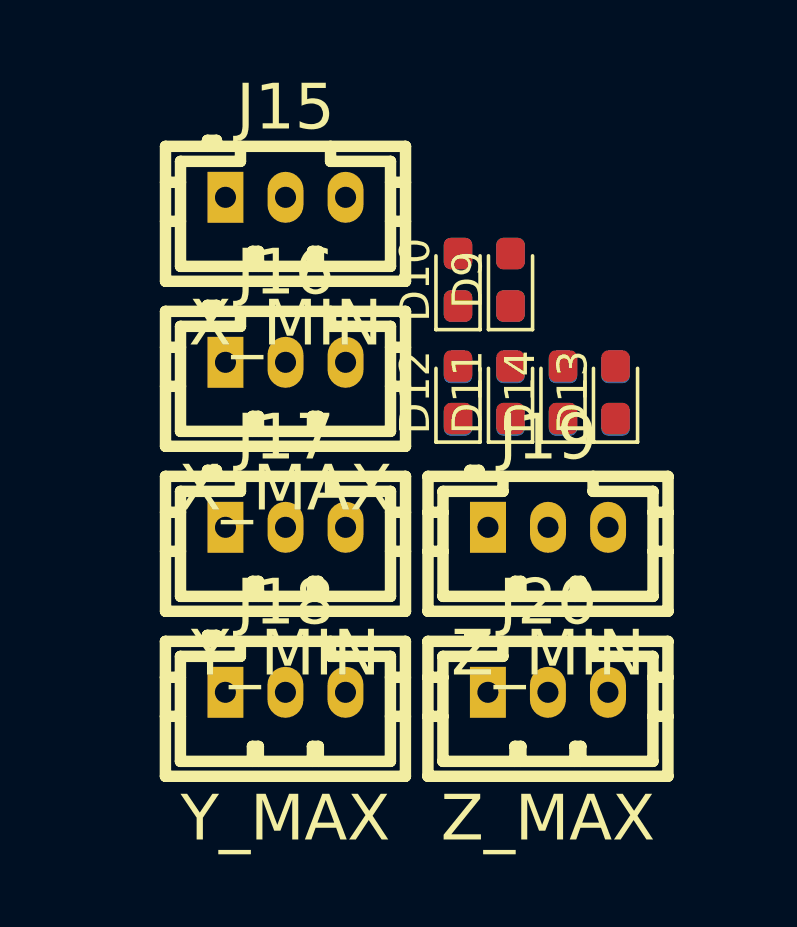
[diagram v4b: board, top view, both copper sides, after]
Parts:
- moved D14 11.2 mm to (17.5, 8.50)
- moved R34 11.0 mm to (17.5, 8.54)
- moved D12 10.6 mm to (14.0, 8.50)
- moved R32 10.6 mm to (14.0, 8.54)
- moved D11 7.25 mm to (15.8, 8.50)
- moved R31 7.22 mm to (15.8, 8.54)
- moved D13 5.96 mm to (19.2, 8.50)
- moved R33 5.93 mm to (19.2, 8.54)
- moved D9 5.40 mm to (15.8, 4.75)
- moved R29 5.40 mm to (15.8, 4.75)
- moved D10 5.13 mm to (14.0, 4.75)
- moved R30 5.13 mm to (14.0, 4.75)
- moved J15 3.40 mm to (8.25, 2.00)
- moved J16 3.29 mm to (8.25, 7.50)
- moved J18 3.29 mm to (8.25, 18.5)
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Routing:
- net +3V3_STM32: track 50.7 -> 0.00 mm
- net GND: track 20.0 -> 0.00 mm
- net /Z_MIN: track 7.88 -> 0.00 mm
- net /Z_MAX: track 7.88 -> 0.00 mm
- net /Y_MAX: track 7.88 -> 0.00 mm
- net /Y_MIN: track 7.88 -> 0.00 mm
- net /X_MIN: track 7.88 -> 0.00 mm
- net /X_MAX: track 7.88 -> 0.00 mm
- net Net-(D10-Pad2): track 3.25 -> 0.00 mm, vias 1 -> 0
- net Net-(D14-Pad2): track 2.96 -> 0.00 mm, vias 1 -> 0
- net Net-(D12-Pad2): track 2.24 -> 0.00 mm, vias 1 -> 0
- net Net-(D13-Pad2): track 2.21 -> 0.00 mm, vias 1 -> 0
- net Net-(D9-Pad2): track 2.21 -> 0.00 mm, vias 1 -> 0
- net Net-(D11-Pad2): track 2.21 -> 0.00 mm, vias 1 -> 0

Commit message: update,
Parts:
- added H1: MOUNT_M3, MountingHole:MountingHole_2.7mm_M2.5, F.Cu at (3.00, 3.00)
- added H2: MOUNT_M3, MountingHole:MountingHole_2.7mm_M2.5, F.Cu at (97.0, 3.00)
- added H3: MOUNT_M3, MountingHole:MountingHole_2.7mm_M2.5, F.Cu at (3.00, 97.0)
- added H4: MOUNT_M3, MountingHole:MountingHole_2.7mm_M2.5, F.Cu at (97.0, 97.0)
- moved R32 81.4 mm to (95.4, 9.30)
- moved D12 81.4 mm to (95.4, 9.30)
- moved D13 79.7 mm to (98.9, 9.30)
- moved D14 79.7 mm to (97.2, 9.30)
- moved R33 79.7 mm to (98.9, 9.30)
- moved R34 79.7 mm to (97.2, 9.30)
- moved R30 78.1 mm to (91.9, 9.25)
- moved D10 78.0 mm to (91.9, 9.25)
- moved R31 77.9 mm to (93.7, 9.30)
- moved D11 77.9 mm to (93.7, 9.30)
- moved J20 77.5 mm to (94.5, 19.5)
- moved J19 77.5 mm to (94.5, 13.5)
- moved J18 76.8 mm to (85.0, 19.5)
- moved J17 76.8 mm to (85.0, 13.8)
- moved J16 76.8 mm to (85.0, 8.00)
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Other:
- board outline added: 100 x 100 mm
